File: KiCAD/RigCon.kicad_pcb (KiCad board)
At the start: 2 copper layers, 35.8 x 77 mm, 79 parts, among them J1 USB_C_Receptacle_USB2.0_16P, J2 PJ-320A, J3 PJ-320A, Q1 MMBT5551L, Q2 MMBT5551L, U1 UC EXPANSION, U10 USBLC6-2P6, U11 CH334P, U2 Speaker, U3 Speaker, U4 CP2102N-A02-GQFN24, U5 CM108B, U6 ADM3101E, U7 PCF8523T, U9 TPS2553, Y1 12MHz, Y3 32,768 kHz

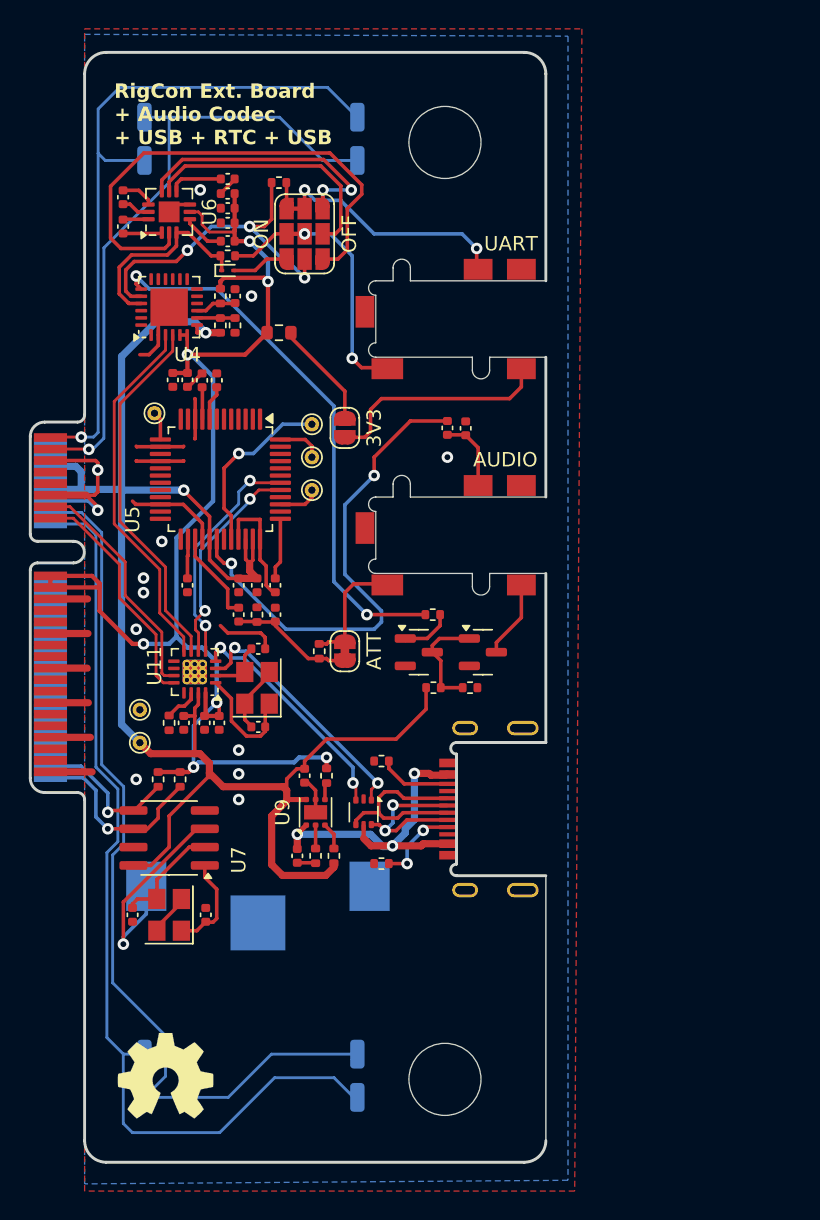
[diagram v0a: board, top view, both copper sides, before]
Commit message: Updated PCB: routing added fox logo correct symbol for mounting hole with pad
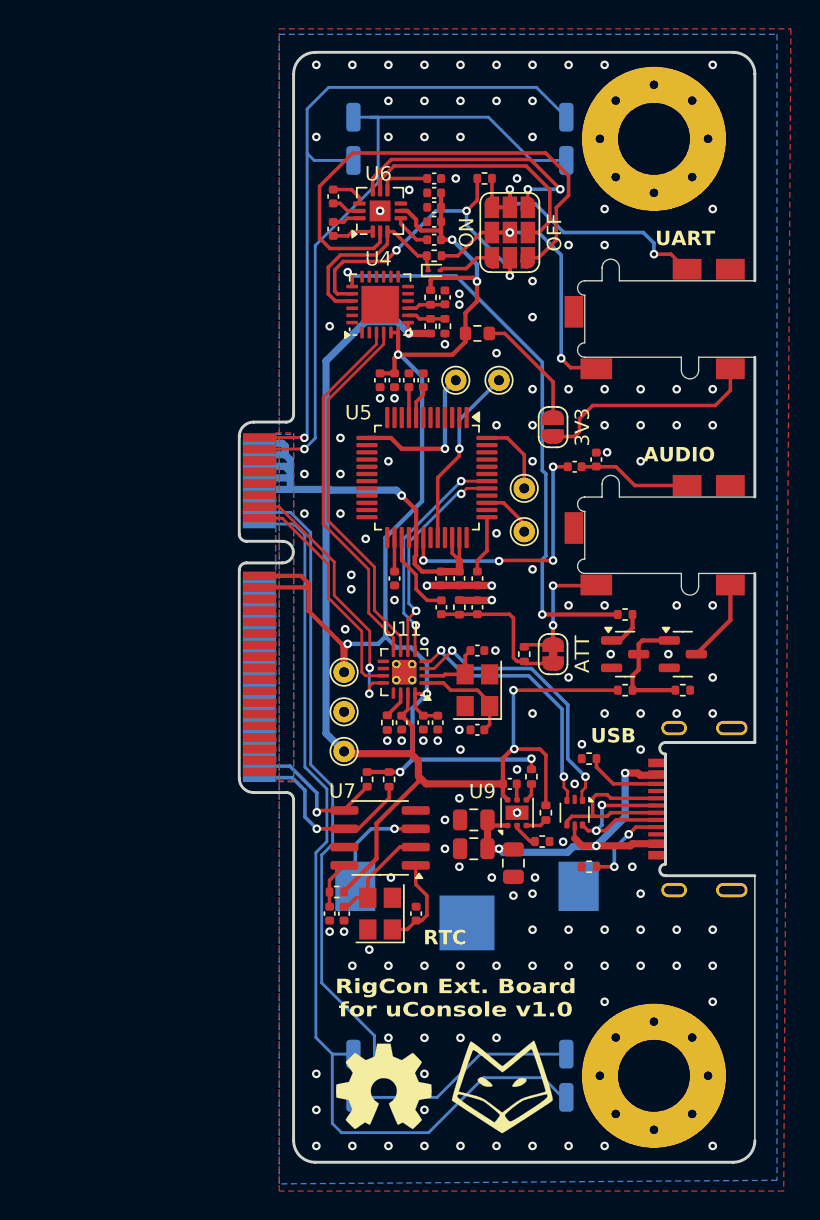
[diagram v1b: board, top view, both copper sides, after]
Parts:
- added C30: 4.7uF, Capacitor_SMD:C_0402_1005Metric, F.Cu at (102.5, 121.2)
- added C31: 47uF, Capacitor_SMD:C_0805_2012Metric, F.Cu at (112.5, 116.8)
- added C32: 47uF, Capacitor_SMD:C_0805_2012Metric, F.Cu at (112.5, 114.8)
- added L2: ~, uconsole:Logo_Fox, F.Cu at (115.5, 137.0)
- added R7: 1k, Resistor_SMD:R_0402_1005Metric, F.Cu at (103.0, 119.8)
- added TP7: 3V3, TestPoint:TestPoint_THTPad_D1.5mm_Drill0.7mm, F.Cu at (103.5, 104.5)
- BT1: footprint BK_940:MPD_BK-940 -> uconsole:MPD_BK-940
- C28: value 100uF -> 47uF; footprint Capacitor_SMD:C_0402_1005Metric -> Capacitor_SMD:C_0805_2012Metric
- H1, H2: footprint MountingHole:MountingHole_5mm -> MountingHole:MountingHole_5mm_Pad_Via
- R22: value 100k -> 47k
- R4: value 100K -> 100k
- TP1, TP2, TP3, TP4, TP5, TP6: footprint footprints:TP -> TestPoint:TestPoint_THTPad_D1.5mm_Drill0.7mm
- moved TP3 21.0 mm to (111.2, 84.2)
- moved R22 15.8 mm to (117.2, 116.2), turned to 0 degrees
- moved Y1 15.3 mm to (112.8, 105.8)
- moved C6 15.2 mm to (112.8, 108.5)
- moved C7 15.2 mm to (112.8, 103.0)
- moved C9 15.2 mm to (109.0, 108.0)
- moved C12 15.2 mm to (110.0, 108.0)
- moved L1 15.2 mm to (106.2, 133.2)
- moved R6 15.1 mm to (106.5, 108.0)
- moved C29 15.1 mm to (107.5, 108.0)
- moved TP5 15.0 mm to (116.0, 94.8)
- moved R3 15.0 mm to (117.5, 114.2), turned to -90 degrees
- moved C28 15.0 mm to (115.2, 117.8)
- moved TP4 14.9 mm to (116.0, 91.8)
- moved R18 14.8 mm to (127.0, 105.8)
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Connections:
- U11 pad 11: /USB4_D+ -> /USB4_D-
- U11 pad 12: /USB4_D- -> /USB4_D+
- U7 pad 8: +5V -> Net-(U7-VDD)
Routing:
- net GND: track 78.1 -> 8.02 mm, vias 13 -> 146
- net Net-(U5-LOL): track 34.8 -> 18.1 mm, vias 2 -> 4
- net /PTT: track 2.25 -> 10.8 mm, vias 0 -> 1
- net Net-(U7-VBAT): track 15.3 -> 7.54 mm
- net /VBUS: track 23.2 -> 27.2 mm
- net Net-(U7-VDD): track 0.00 -> 3.30 mm
- net /RIG_AFIN: track 5.13 -> 7.86 mm
- net /COS: track 3.14 -> 5.40 mm
- net RTS: track 38.0 -> 40.2 mm
- net Net-(JP3-A): track 8.68 -> 10.8 mm
- net /USB4_D+: track 16.4 -> 18.5 mm, vias 0 -> 2
- net EXT_P: track 16.1 -> 18.1 mm
- net EXT_N: track 17.7 -> 19.2 mm
- net Net-(U11-XO): track 8.53 -> 7.09 mm
- net +5V: track 121.1 -> 119.9 mm, vias 2 -> 4
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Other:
- board text added: "CR1220"
- board text added: "RTC"
- board text added: "RigCon Ext. Board for uConsole v1.0"
- board text added: "USB"
- board text removed: "RigCon Ext. Board + Audio Codec + USB + RTC + USB"

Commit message: Removed DigiRig Footprint Library Added github URL on silkscreen
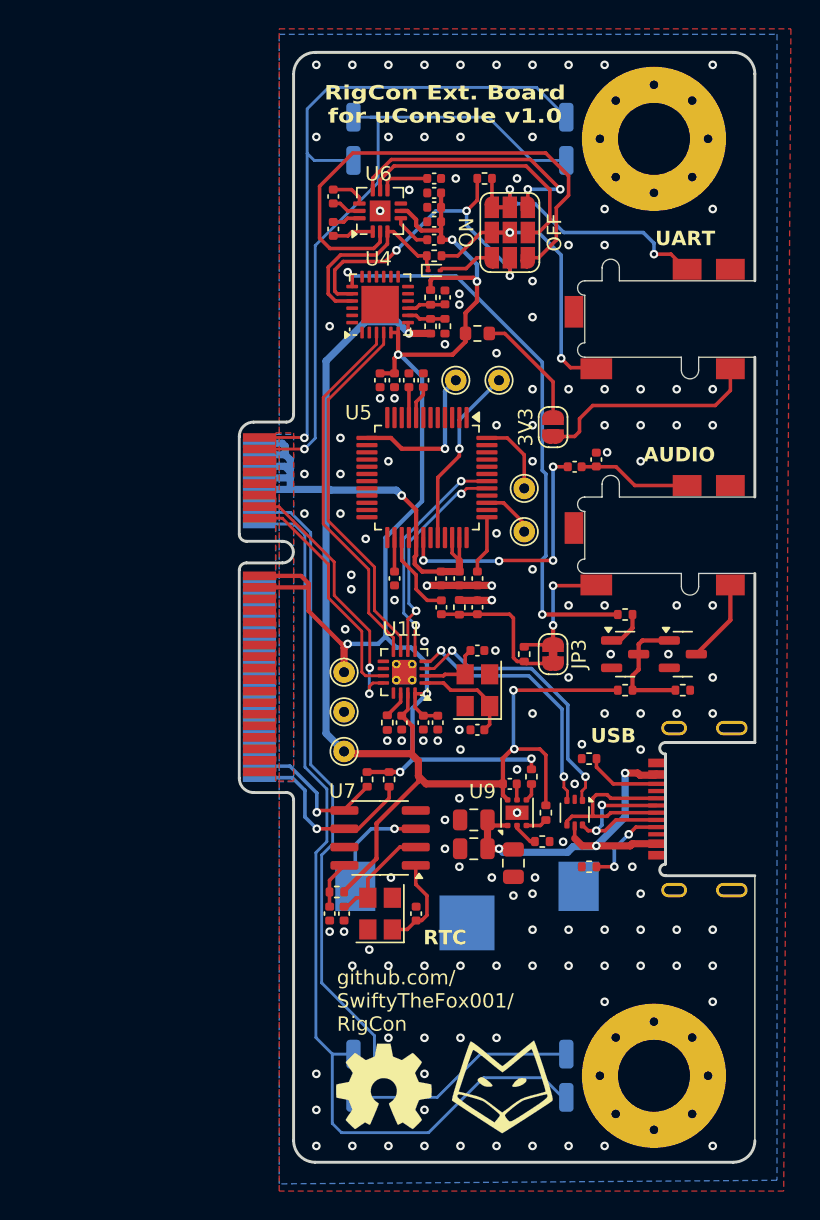
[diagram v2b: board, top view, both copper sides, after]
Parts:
- JP1: footprint footprints:SolderJumper9-BCu -> uconsole:SolderJumper9-BCu
- JP2: footprint footprints:SolderJumper2-BCu -> uconsole:SolderJumper2-BCu
- JP3: footprint footprints:SolderJumper-BCu-Bridged -> uconsole:SolderJumper-BCu-Bridged
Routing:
- net GND: vias 146 -> 141
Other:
- board text added: "github.com/ SwiftyTheFox001/ RigCon"

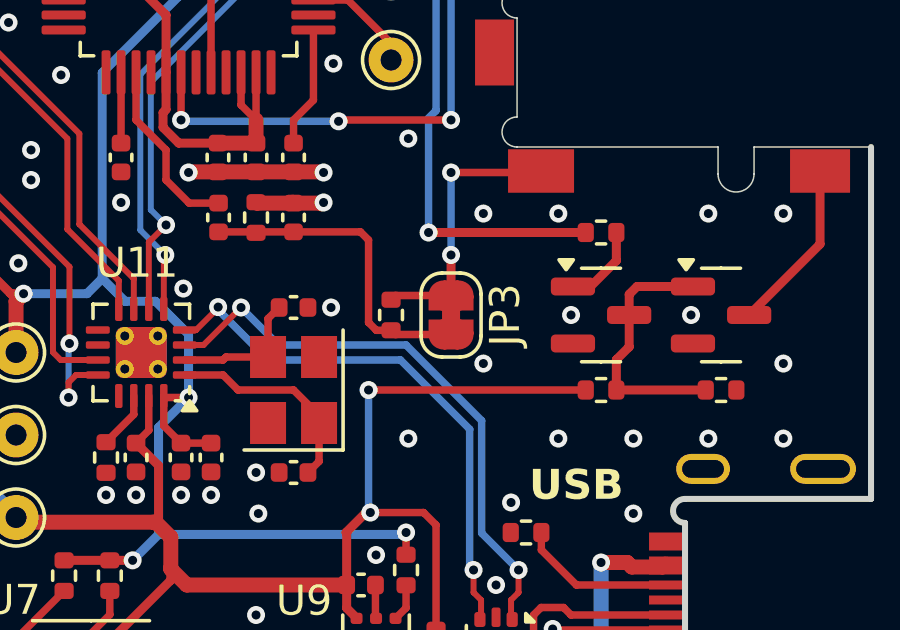
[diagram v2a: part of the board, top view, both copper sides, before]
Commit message: Fixed Errors in Labels excluded parts from position file and bom
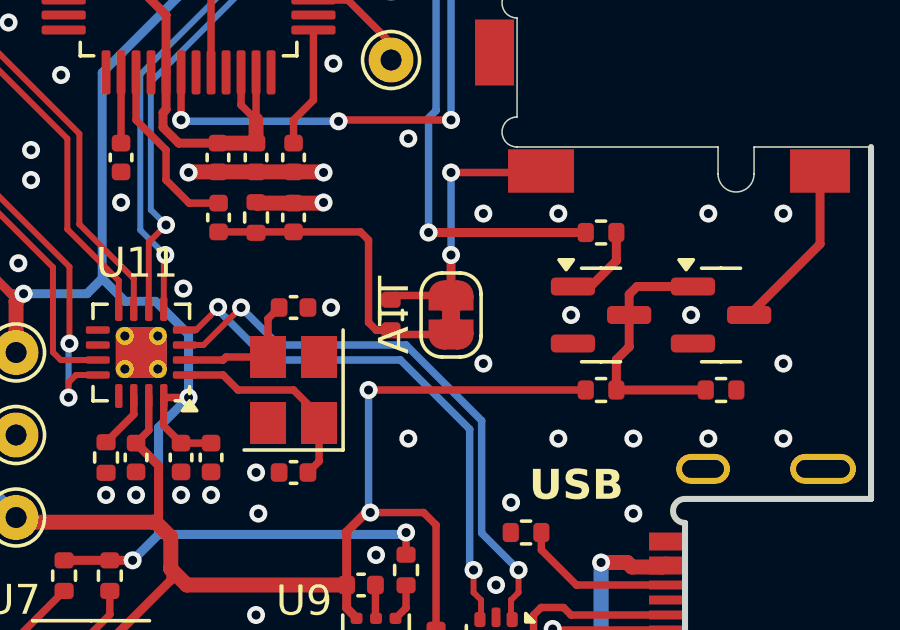
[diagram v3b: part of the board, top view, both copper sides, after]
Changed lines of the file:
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@@
 	(paper "A4")
 	(title_block
-		(title "uConsole expansion card template")
-		(date "2024-07-10")
-		(rev "0.1")
+		(title "RigCon Extension Board for ClockworkPi uConsole")
+		(date "2025-02-26")
+		(rev "1.0")
 	)
 	(layers
@@
 		(sheetname "Stammblatt")
 		(sheetfile "RigCon.kicad_sch")
-		(attr smd exclude_from_bom)
+		(attr smd exclude_from_pos_files exclude_from_bom)
 		(fp_line
 			(start 4.62 -6.2)
@@
 		(sheetname "Stammblatt")
 		(sheetfile "RigCon.kicad_sch")
-		(attr through_hole)
+		(attr through_hole exclude_from_pos_files exclude_from_bom)
 		(fp_poly
 			(pts
@@
 		(sheetname "Stammblatt")
 		(sheetfile "RigCon.kicad_sch")
-		(attr smd exclude_from_pos_files allow_soldermask_bridges)
+		(attr smd exclude_from_pos_files exclude_from_bom allow_soldermask_bridges)
 		(fp_rect
 			(start -0.6096 -13.716)
@@
 		(sheetname "Stammblatt")
 		(sheetfile "RigCon.kicad_sch")
-		(attr smd exclude_from_bom)
+		(attr smd exclude_from_pos_files exclude_from_bom)
 		(fp_line
 			(start 11.8 -1.65)
@@
 		(sheetname "Stammblatt")
 		(sheetfile "RigCon.kicad_sch")
-		(attr smd exclude_from_bom)
+		(attr smd exclude_from_pos_files exclude_from_bom)
 		(fp_line
 			(start 11.8 -1.65)
@@
 		(sheetname "Stammblatt")
 		(sheetfile "RigCon.kicad_sch")
-		(attr smd exclude_from_pos_files)
+		(attr smd exclude_from_pos_files exclude_from_bom)
 		(fp_rect
 			(start -8.2 4.7)
@@
 			(at -3.325 7.135 180)
 			(layer "B.SilkS")
+			(hide yes)
 			(effects
 				(font
@@
 			(at 0 1.8 -90)
 			(layer "F.SilkS")
+			(hide yes)
 			(effects
 				(font
@@
 		(property "Value" "ATT"
 			(at 0 -1.9 -90)
-			(layer "F.Fab")
+			(layer "F.SilkS")
 			(effects
 				(font
@@
 		(sheetname "Stammblatt")
 		(sheetfile "RigCon.kicad_sch")
-		(attr smd exclude_from_pos_files)
+		(attr smd exclude_from_pos_files exclude_from_bom)
 		(fp_rect
 			(start -8.2 4.7)

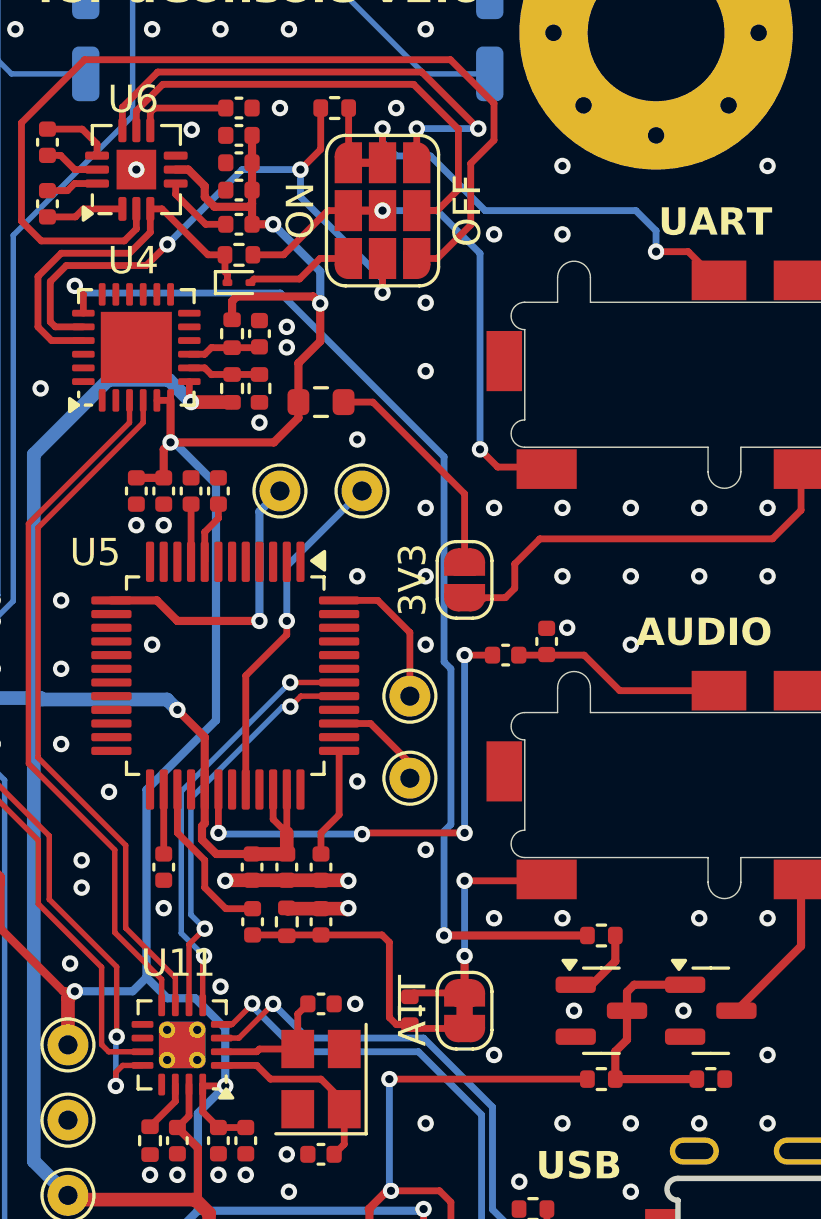
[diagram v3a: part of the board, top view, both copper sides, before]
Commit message: Version of prototype order (v1.0)
Updated a few Texts and Order Numbers
Updated TPS2553 to TPS2553-1 (Latched version)
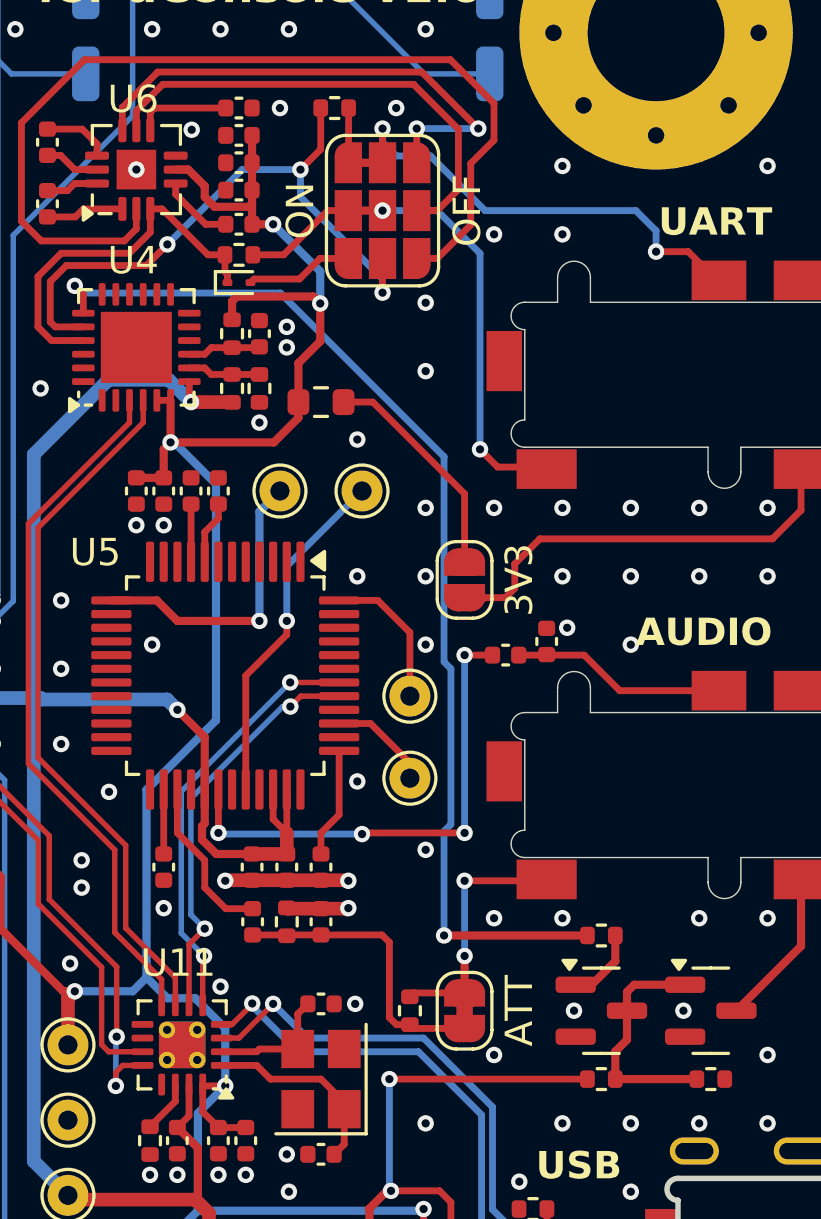
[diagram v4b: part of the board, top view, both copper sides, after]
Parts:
- C6, C7: value 27pF -> 10pF
- U9: value TPS2553 -> TPS2553-1
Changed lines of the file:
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@@
 			)
 		)
-		(property "Value" "27pF"
+		(property "Value" "10pF"
 			(at 0 1.16 0)
 			(layer "F.Fab")
@@
 			)
 		)
-		(property "Value" "27pF"
+		(property "Value" "10pF"
 			(at 0 1.16 0)
 			(layer "F.Fab")
@@
 			)
 		)
-		(property "Value" "TPS2553"
+		(property "Value" "TPS2553-1"
 			(at 0 1.95 90)
 			(layer "F.Fab")
@@
 			)
 		)
-		(property "LCSC" "C521201"
+		(property "LCSC" "C411878 "
 			(at 0 0 90)
 			(unlocked yes)
@@
 				(font
 					(size 1 1)
-					(thickness 0.15)
+					(thickness 0.153)
 				)
 			)
@@
 				(font
 					(size 1 1)
-					(thickness 0.15)
+					(thickness 0.153)
 				)
 			)
@@
 			(end -6.605 -2.026)
 			(stroke
-				(width 0.127)
+				(width 0.153)
 				(type solid)
 			)
@@
 			(end -6.605 2.3739)
 			(stroke
-				(width 0.127)
+				(width 0.153)
 				(type solid)
 			)
@@
 			(end -3.0734 5.9055)
 			(stroke
-				(width 0.127)
+				(width 0.153)
 				(type solid)
 			)
@@
 			(end -3.0734 5.9055)
 			(stroke
-				(width 0.127)
+				(width 0.153)
 				(type solid)
 			)
@@
 			(end -6.605 -6.6929)
 			(stroke
-				(width 0.127)
+				(width 0.153)
 				(type solid)
 			)
@@
 			(end 6.605 -2.026)
 			(stroke
-				(width 0.127)
+				(width 0.153)
 				(type solid)
 			)
@@
 			(end 6.605 2.3739)
 			(stroke
-				(width 0.127)
+				(width 0.153)
 				(type solid)
 			)
@@
 			(end 3.0734 5.9055)
 			(stroke
-				(width 0.127)
+				(width 0.153)
 				(type solid)
 			)
@@
 			(end 8 -2.5)
 			(stroke
-				(width 0.127)
+				(width 0.2)
 				(type solid)
 			)
@@
 			(end 7.5 -3)
 			(stroke
-				(width 0.127)
+				(width 0.2)
 				(type solid)
 			)
@@
 		)
 		(fp_line
-			(start -10 -0.5)
-			(end -10 0.5)
+			(start -6.605 -6.6929)
+			(end -6.605 2.3739)
 			(stroke
 				(width 0.127)
@@
 		)
 		(fp_line
-			(start -9.5 0)
-			(end -10.5 0)
+			(start -6.605 2.3739)
+			(end -3.0734 5.9055)
 			(stroke
 				(width 0.127)
@@
 		)
 		(fp_line
-			(start -6.605 -6.6929)
-			(end -6.605 2.3739)
+			(start 3.0734 5.9055)
+			(end -3.0734 5.9055)
 			(stroke
 				(width 0.127)
@@
 		)
 		(fp_line
-			(start -6.605 2.3739)
-			(end -3.0734 5.9055)
+			(start 6.605 -6.6929)
+			(end -6.605 -6.6929)
 			(stroke
 				(width 0.127)
@@
 		)
 		(fp_line
-			(start 3.0734 5.9055)
-			(end -3.0734 5.9055)
+			(start 6.605 -6.6929)
+			(end 6.605 2.3739)
 			(stroke
 				(width 0.127)
@@
 		)
 		(fp_line
-			(start 6.605 -6.6929)
-			(end -6.605 -6.6929)
+			(start 6.605 2.3739)
+			(end 3.0734 5.9055)
 			(stroke
 				(width 0.127)
@@
 		)
 		(fp_line
-			(start 6.605 -6.6929)
-			(end 6.605 2.3739)
+			(start 8 -3.5)
+			(end 8 -2.5)
 			(stroke
 				(width 0.127)
@@
 		)
 		(fp_line
-			(start 6.605 2.3739)
-			(end 3.0734 5.9055)
+			(start 8.5 -3)
+			(end 7.5 -3)
 			(stroke
 				(width 0.127)
@@
 			(at -7.7475 0)
 			(size 2.785 3.425)
-			(layers "B.Cu" "B.Paste" "B.Mask")
+			(layers "B.Cu" "B.Mask")
 			(net 54 "Net-(U7-VBAT)")
 			(pintype "passive")
@@
 			(at 7.7475 0)
 			(size 2.785 3.425)
-			(layers "B.Cu" "B.Paste" "B.Mask")
+			(layers "B.Cu" "B.Mask")
 			(net 136 "unconnected-(BT1-PadP2)")
 			(pintype "passive+no_connect")
 			(solder_mask_margin 0.102)
 		)
+		(model "${KIPRJMOD}/BK_940/BK-940.step"
+			(offset
+				(xyz 0 0 0)
+			)
+			(scale
+				(xyz 1 1 1)
+			)
+			(rotate
+				(xyz -90 0 0)
+			)
+		)
 	)
 	(footprint "uconsole:SolderJumper-BCu-Bridged"
@@
 		)
 		(property "Value" "ATT"
-			(at 0 -1.9 -90)
+			(at 0 2 -90)
 			(layer "F.SilkS")
 			(effects
 				(font
 					(size 1 1)
-					(thickness 0.15)
+					(thickness 0.153)
 				)
 			)
@@
 		)
 		(property "Value" "3V3"
-			(at 0 -1.9 -90)
+			(at 0 2 -90)
 			(layer "F.SilkS")
 			(effects
 				(font
 					(size 1 1)
-					(thickness 0.15)
+					(thickness 0.153)
 				)
 			)
